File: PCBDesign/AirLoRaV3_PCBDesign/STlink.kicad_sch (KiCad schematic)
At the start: 1 part, among them J6 UART2

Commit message: Update circiut
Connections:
- net 3.3V renamed +3.3V
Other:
- moved on the sheet: J6
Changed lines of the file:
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@@
 	(generator_version "8.0")
 	(paper "A4")
-	(rectangle
-		(start 96.52 54.61)
-		(end 130.81 78.74)
+	(wire
+		(pts
+			(xy 142.24 100.33) (xy 157.48 100.33)
+		)
 		(stroke
 			(width 0)
 			(type default)
 		)
+	)
+	(rectangle
+		(start 129.54 83.82)
+		(end 163.83 107.95)
+		(stroke
+			(width 0)
+			(type default)
+		)
 		(fill
 			(type none)
@@
 	(text "STLink"
 		(exclude_from_sim no)
-		(at 113.538 56.642 0)
+		(at 146.558 85.852 0)
 		(effects
 			(font
@@
 	(hierarchical_label "T_SWCLK"
 		(shape input)
-		(at 115.57 69.85 0)
+		(at 142.24 97.79 0)
 		(fields_autoplaced yes)
 		(effects
@@
 	(hierarchical_label "T_SWDIO"
 		(shape input)
-		(at 115.57 67.31 0)
+		(at 142.24 95.25 0)
 		(fields_autoplaced yes)
 		(effects
@@
 		)
 	)
-	(hierarchical_label "3.3V"
-		(shape input)
-		(at 115.57 72.39 0)
-		(fields_autoplaced yes)
-		(effects
-			(font
-				(size 1.27 1.27)
-			)
-			(justify left)
-		)
-	)
 	(symbol
 		(lib_id "Connector:Screw_Terminal_01x04")
-		(at 110.49 72.39 180)
+		(at 137.16 100.33 180)
 		(unit 1)
 		(exclude_from_sim no)
@@
 		(fields_autoplaced yes)
 		(property "Reference" "J6"
-			(at 110.49 60.96 0)
+			(at 137.16 88.9 0)
 			(effects
 				(font
@@
 		)
 		(property "Value" "UART2"
-			(at 110.49 63.5 0)
+			(at 137.16 91.44 0)
 			(effects
 				(font
@@
 		)
 		(property "Footprint" "Connector_JST:JST_XH_B4B-XH-A_1x04_P2.50mm_Vertical"
-			(at 110.49 72.39 0)
+			(at 137.16 100.33 0)
 			(effects
 				(font
@@
 		)
 		(property "Datasheet" "~"
-			(at 110.49 72.39 0)
+			(at 137.16 100.33 0)
 			(effects
 				(font
@@
 		)
 		(property "Description" ""
-			(at 110.49 72.39 0)
+			(at 137.16 100.33 0)
 			(effects
 				(font
@@
 	(symbol
 		(lib_id "power:GND")
-		(at 115.57 74.93 90)
+		(at 142.24 102.87 90)
 		(unit 1)
 		(exclude_from_sim no)
@@
 		(fields_autoplaced yes)
 		(property "Reference" "#PWR043"
-			(at 121.92 74.93 0)
+			(at 148.59 102.87 0)
 			(effects
 				(font
@@
 		)
 		(property "Value" "GND"
-			(at 119.38 74.9299 90)
+			(at 146.05 102.8699 90)
 			(effects
 				(font
@@
 		)
 		(property "Footprint" ""
-			(at 115.57 74.93 0)
+			(at 142.24 102.87 0)
 			(effects
 				(font
@@
 		)
 		(property "Datasheet" ""
-			(at 115.57 74.93 0)
+			(at 142.24 102.87 0)
 			(effects
 				(font
@@
 		)
 		(property "Description" "Power symbol creates a global label with name \"GND\" , ground"
-			(at 115.57 74.93 0)
+			(at 142.24 102.87 0)
 			(effects
 				(font
@@
 					(unit 1)
 				)
+			)
+		)
+	)
+	(symbol
+		(lib_id "power:+3.3V")
+		(at 157.48 100.33 0)
+		(unit 1)
+		(exclude_from_sim no)
+		(in_bom yes)
+		(on_board yes)
+		(dnp no)
+		(fields_autoplaced yes)
+		(property "Reference" "#PWR044"
+			(at 157.48 104.14 0)
+			(effects
+				(font
+					(size 1.27 1.27)
+				)
+				(hide yes)
+			)
+		)
+		(property "Value" "+3.3V"
+			(at 157.48 95.25 0)
+			(effects
+				(font
+					(size 1.27 1.27)
+				)
+			)
+		)
+		(property "Footprint" ""
+			(at 157.48 100.33 0)
+			(effects
+				(font
+					(size 1.27 1.27)
+				)
+				(hide yes)
+			)
+		)
+		(property "Datasheet" ""
+			(at 157.48 100.33 0)
+			(effects
+				(font
+					(size 1.27 1.27)
+				)
+				(hide yes)
+			)
+		)
+		(property "Description" "Power symbol creates a global label with name \"+3.3V\""
+			(at 157.48 100.33 0)
+			(effects
+				(font
+					(size 1.27 1.27)
+				)
+				(hide yes)
+			)
+		)
+		(pin "1"
+		)
+		(instances
+			(project "airlora-kicad"
+				(path "/59d971df-d6c1-4ef7-a085-bf08b7b16047/be77b740-d58b-414b-97ce-61f1d1685314/0fe76900-3fef-41a8-aa6f-27268a6f6f64"
+					(reference "#PWR044")
+					(unit 1)
+				)

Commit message: Update PCB layout
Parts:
- renumbered J6 to J7
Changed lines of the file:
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@@
 		(dnp no)
 		(fields_autoplaced yes)
-		(property "Reference" "J6"
+		(property "Reference" "J7"
 			(at 137.16 88.9 0)
 			(effects
@@
 			(project "airlora-kicad"
 				(path "/59d971df-d6c1-4ef7-a085-bf08b7b16047/be77b740-d58b-414b-97ce-61f1d1685314/0fe76900-3fef-41a8-aa6f-27268a6f6f64"
-					(reference "J6")
+					(reference "J7")
 					(unit 1)
 				)

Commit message: Update schematic
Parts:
- added SW2: SW_Slide_DPDT, Button_Switch_THT:SW_E-Switch_EG1271_SPDT, symbol Switch:SW_Slide_DPDT
- renumbered J7 to J8
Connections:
- net T_SWCLK: now also SW2.6 (C); no longer J8.3 (Pin_3)
- net T_SWDIO: now also SW2.1 (A); no longer J8.4 (Pin_4)
- new net: J8.3 (Pin_3), SW2.2 (B)
- new net: J8.4 (Pin_4), SW2.5 (B)
- new net T_SWCLK1: SW2.4 (A)
- new net T_SWDIO1: SW2.3 (C)
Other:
- moved on the sheet: J8
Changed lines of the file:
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@@
 	(wire
 		(pts
-			(xy 142.24 100.33) (xy 157.48 100.33)
+			(xy 147.32 77.47) (xy 147.32 85.09)
+		)
+		(stroke
+			(width 0)
+			(type default)
+		)
+	)
+	(wire
+		(pts
+			(xy 147.32 85.09) (xy 139.7 85.09)
+		)
+		(stroke
+			(width 0)
+			(type default)
+		)
+	)
+	(wire
+		(pts
+			(xy 147.32 88.9) (xy 163.83 88.9)
+		)
+		(stroke
+			(width 0)
+			(type default)
+		)
+	)
+	(wire
+		(pts
+			(xy 147.32 87.63) (xy 139.7 87.63)
+		)
+		(stroke
+			(width 0)
+			(type default)
+		)
+	)
+	(wire
+		(pts
+			(xy 186.69 88.9) (xy 186.69 77.47)
+		)
+		(stroke
+			(width 0)
+			(type default)
+		)
+	)
+	(wire
+		(pts
+			(xy 186.69 77.47) (xy 147.32 77.47)
+		)
+		(stroke
+			(width 0)
+			(type default)
+		)
+	)
+	(wire
+		(pts
+			(xy 147.32 88.9) (xy 147.32 87.63)
+		)
+		(stroke
+			(width 0)
+			(type default)
+		)
+	)
+	(wire
+		(pts
+			(xy 173.99 88.9) (xy 186.69 88.9)
 		)
 		(stroke
@@
 	)
 	(rectangle
-		(start 129.54 83.82)
-		(end 163.83 107.95)
+		(start 126.365 66.04)
+		(end 191.135 100.33)
 		(stroke
 			(width 0)
@@
 	(text "STLink"
 		(exclude_from_sim no)
-		(at 146.558 85.852 0)
+		(at 159.766 72.644 0)
 		(effects
 			(font
@@
 		)
 	)
-	(hierarchical_label "T_SWCLK"
+	(hierarchical_label "T_SWCLK1"
 		(shape input)
-		(at 142.24 97.79 0)
+		(at 173.99 93.98 0)
 		(fields_autoplaced yes)
 		(effects
@@
 		)
 	)
-	(hierarchical_label "T_SWDIO"
+	(hierarchical_label "T_SWCLK"
 		(shape input)
-		(at 142.24 95.25 0)
+		(at 173.99 83.82 0)
 		(fields_autoplaced yes)
 		(effects
@@
 		)
 	)
+	(hierarchical_label "T_SWDIO"
+		(shape input)
+		(at 163.83 83.82 180)
+		(fields_autoplaced yes)
+		(effects
+			(font
+				(size 1.27 1.27)
+			)
+			(justify right)
+		)
+	)
+	(hierarchical_label "T_SWDIO1"
+		(shape input)
+		(at 163.83 93.98 180)
+		(fields_autoplaced yes)
+		(effects
+			(font
+				(size 1.27 1.27)
+			)
+			(justify right)
+		)
+	)
 	(symbol
 		(lib_id "Connector:Screw_Terminal_01x04")
-		(at 137.16 100.33 180)
+		(at 134.62 90.17 180)
 		(unit 1)
 		(exclude_from_sim no)
@@
 		(dnp no)
 		(fields_autoplaced yes)
-		(property "Reference" "J7"
-			(at 137.16 88.9 0)
+		(property "Reference" "J8"
+			(at 134.62 78.74 0)
 			(effects
 				(font
@@
 		)
 		(property "Value" "UART2"
-			(at 137.16 91.44 0)
+			(at 134.62 81.28 0)
 			(effects
 				(font
@@
 		)
 		(property "Footprint" "Connector_JST:JST_XH_B4B-XH-A_1x04_P2.50mm_Vertical"
-			(at 137.16 100.33 0)
+			(at 134.62 90.17 0)
 			(effects
 				(font
@@
 		)
 		(property "Datasheet" "~"
-			(at 137.16 100.33 0)
+			(at 134.62 90.17 0)
 			(effects
 				(font
@@
 		)
 		(property "Description" ""
-			(at 137.16 100.33 0)
+			(at 134.62 90.17 0)
 			(effects
 				(font
@@
 		)
 		(property "MANUFACTURER" ""
-			(at 137.16 100.33 0)
+			(at 134.62 90.17 0)
 			(effects
 				(font
@@
 		)
 		(property "MAXIMUM_PACKAGE_HEIGHT" ""
-			(at 137.16 100.33 0)
+			(at 134.62 90.17 0)
 			(effects
 				(font
@@
 		)
 		(property "PARTREV" ""
-			(at 137.16 100.33 0)
+			(at 134.62 90.17 0)
 			(effects
 				(font
@@
 		)
 		(property "STANDARD" ""
-			(at 137.16 100.33 0)
+			(at 134.62 90.17 0)
 			(effects
 				(font
@@
 			(project "airlora-kicad"
 				(path "/59d971df-d6c1-4ef7-a085-bf08b7b16047/be77b740-d58b-414b-97ce-61f1d1685314/0fe76900-3fef-41a8-aa6f-27268a6f6f64"
-					(reference "J7")
+					(reference "J8")
 					(unit 1)
 				)
@@
 	(symbol
 		(lib_id "power:GND")
-		(at 142.24 102.87 90)
+		(at 139.7 92.71 90)
 		(unit 1)
 		(exclude_from_sim no)
@@
 		(dnp no)
 		(fields_autoplaced yes)
-		(property "Reference" "#PWR043"
-			(at 148.59 102.87 0)
+		(property "Reference" "#PWR046"
+			(at 146.05 92.71 0)
 			(effects
 				(font
@@
 		)
 		(property "Value" "GND"
-			(at 146.05 102.8699 90)
+			(at 143.51 92.7099 90)
 			(effects
 				(font
@@
 		)
 		(property "Footprint" ""
-			(at 142.24 102.87 0)
+			(at 139.7 92.71 0)
 			(effects
 				(font
@@
 		)
 		(property "Datasheet" ""
-			(at 142.24 102.87 0)
+			(at 139.7 92.71 0)
 			(effects
 				(font
@@
 		)
 		(property "Description" "Power symbol creates a global label with name \"GND\" , ground"
-			(at 142.24 102.87 0)
+			(at 139.7 92.71 0)
 			(effects
 				(font
@@
 			(project "airlora-kicad"
 				(path "/59d971df-d6c1-4ef7-a085-bf08b7b16047/be77b740-d58b-414b-97ce-61f1d1685314/0fe76900-3fef-41a8-aa6f-27268a6f6f64"
-					(reference "#PWR043")
+					(reference "#PWR046")
 					(unit 1)
 				)
@@
 	(symbol
 		(lib_id "power:+3.3V")
-		(at 157.48 100.33 0)
+		(at 139.7 90.17 270)
 		(unit 1)
 		(exclude_from_sim no)
@@
 		(dnp no)
 		(fields_autoplaced yes)
-		(property "Reference" "#PWR044"
-			(at 157.48 104.14 0)
+		(property "Reference" "#PWR045"
+			(at 135.89 90.17 0)
 			(effects
 				(font
@@
 		)
 		(property "Value" "+3.3V"
-			(at 157.48 95.25 0)
-			(effects
-				(font
-					(size 1.27 1.27)
-				)
+			(at 143.51 90.1699 90)
+			(effects
+				(font
+					(size 1.27 1.27)
+				)
+				(justify left)
 			)
 		)
 		(property "Footprint" ""
-			(at 157.48 100.33 0)
+			(at 139.7 90.17 0)
 			(effects
 				(font
@@
 		)
 		(property "Datasheet" ""
-			(at 157.48 100.33 0)
+			(at 139.7 90.17 0)
 			(effects
 				(font
@@
 		)
 		(property "Description" "Power symbol creates a global label with name \"+3.3V\""
-			(at 157.48 100.33 0)
+			(at 139.7 90.17 0)
 			(effects
 				(font
@@
 			(project "airlora-kicad"
 				(path "/59d971df-d6c1-4ef7-a085-bf08b7b16047/be77b740-d58b-414b-97ce-61f1d1685314/0fe76900-3fef-41a8-aa6f-27268a6f6f64"
-					(reference "#PWR044")
+					(reference "#PWR045")
 					(unit 1)
 				)
+			)
+		)
+	)
+	(symbol
+		(lib_id "Switch:SW_Slide_DPDT")
+		(at 168.91 88.9 0)
+		(unit 1)
+		(exclude_from_sim no)
+		(in_bom yes)
+		(on_board yes)
+		(dnp no)
+		(fields_autoplaced yes)
+		(property "Reference" "SW2"
+			(at 168.91 78.74 0)
+			(effects
+				(font
+					(size 1.27 1.27)
+				)
+			)
+		)
+		(property "Value" "SW_Slide_DPDT"
+			(at 168.91 81.28 0)
+			(effects
+				(font
+					(size 1.27 1.27)
+				)
+			)
+		)
+		(property "Footprint" "Button_Switch_THT:SW_E-Switch_EG1271_SPDT"
+			(at 182.88 83.82 0)
+			(effects
+				(font
+					(size 1.27 1.27)
+				)
+				(hide yes)
+			)
+		)
+		(property "Datasheet" "~"
+			(at 168.91 88.9 0)
+			(effects
+				(font
+					(size 1.27 1.27)
+				)
+				(hide yes)
+			)
+		)
+		(property "Description" "Slide Switch, dual pole double throw"
+			(at 168.91 88.9 0)
+			(effects
+				(font
+					(size 1.27 1.27)
+				)
+				(hide yes)
+			)
+		)
+		(pin "6"
+		)
+		(pin "4"
+		)
+		(pin "1"
+		)
+		(pin "3"
+		)
+		(pin "5"
+		)
+		(pin "2"
+		)
+		(instances
+			(project "airlora-kicad"
+				(path "/59d971df-d6c1-4ef7-a085-bf08b7b16047/be77b740-d58b-414b-97ce-61f1d1685314/0fe76900-3fef-41a8-aa6f-27268a6f6f64"
+					(reference "SW2")
+					(unit 1)
+				)

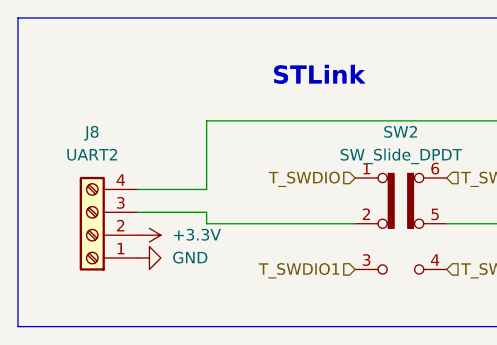
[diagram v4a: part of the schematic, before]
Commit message: Update circuit buck converter and sensor
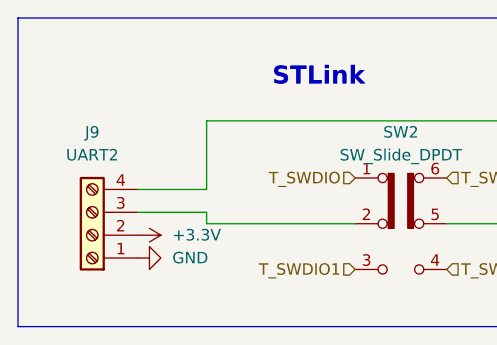
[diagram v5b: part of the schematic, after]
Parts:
- J9: renamed from J8; footprint Connector_JST:JST_XH_B4B-XH-A_1x04_P2.50mm_Vertical -> Connector_Molex:Molex_CLIK-Mate_502585-0470_1x04-1MP_P1.50mm_Horizontal
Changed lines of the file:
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@@
 		(dnp no)
 		(fields_autoplaced yes)
-		(property "Reference" "J8"
+		(property "Reference" "J9"
 			(at 134.62 78.74 0)
 			(effects
@@
 			)
 		)
-		(property "Footprint" "Connector_JST:JST_XH_B4B-XH-A_1x04_P2.50mm_Vertical"
+		(property "Footprint" "Connector_Molex:Molex_CLIK-Mate_502585-0470_1x04-1MP_P1.50mm_Horizontal"
 			(at 134.62 90.17 0)
 			(effects
@@
 			(project "airlora-kicad"
 				(path "/59d971df-d6c1-4ef7-a085-bf08b7b16047/be77b740-d58b-414b-97ce-61f1d1685314/0fe76900-3fef-41a8-aa6f-27268a6f6f64"
-					(reference "J8")
+					(reference "J9")
 					(unit 1)
 				)
@@
 		(dnp no)
 		(fields_autoplaced yes)
-		(property "Reference" "#PWR046"
+		(property "Reference" "#PWR051"
 			(at 146.05 92.71 0)
 			(effects
@@
 			(project "airlora-kicad"
 				(path "/59d971df-d6c1-4ef7-a085-bf08b7b16047/be77b740-d58b-414b-97ce-61f1d1685314/0fe76900-3fef-41a8-aa6f-27268a6f6f64"
-					(reference "#PWR046")
+					(reference "#PWR051")
 					(unit 1)
 				)
@@
 		(dnp no)
 		(fields_autoplaced yes)
-		(property "Reference" "#PWR045"
+		(property "Reference" "#PWR050"
 			(at 135.89 90.17 0)
 			(effects
@@
 			(project "airlora-kicad"
 				(path "/59d971df-d6c1-4ef7-a085-bf08b7b16047/be77b740-d58b-414b-97ce-61f1d1685314/0fe76900-3fef-41a8-aa6f-27268a6f6f64"
-					(reference "#PWR045")
+					(reference "#PWR050")
 					(unit 1)
 				)

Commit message: Update schematic
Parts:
- J9: footprint Connector_Molex:Molex_CLIK-Mate_502585-0470_1x04-1MP_P1.50mm_Horizontal -> Connector_JST:JST_XH_B4B-XH-A_1x04_P2.50mm_Vertical
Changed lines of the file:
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@@
 			)
 		)
-		(property "Footprint" "Connector_Molex:Molex_CLIK-Mate_502585-0470_1x04-1MP_P1.50mm_Horizontal"
+		(property "Footprint" "Connector_JST:JST_XH_B4B-XH-A_1x04_P2.50mm_Vertical"
 			(at 134.62 90.17 0)
 			(effects

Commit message: Update PCB
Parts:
- renumbered J9 to J11
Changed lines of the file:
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@@
 		(dnp no)
 		(fields_autoplaced yes)
-		(property "Reference" "J9"
+		(property "Reference" "J11"
 			(at 134.62 78.74 0)
 			(effects
@@
 			(project "airlora-kicad"
 				(path "/59d971df-d6c1-4ef7-a085-bf08b7b16047/be77b740-d58b-414b-97ce-61f1d1685314/0fe76900-3fef-41a8-aa6f-27268a6f6f64"
-					(reference "J9")
+					(reference "J11")
 					(unit 1)
 				)
@@
 		(dnp no)
 		(fields_autoplaced yes)
-		(property "Reference" "#PWR051"
+		(property "Reference" "#PWR058"
 			(at 146.05 92.71 0)
 			(effects
@@
 			(project "airlora-kicad"
 				(path "/59d971df-d6c1-4ef7-a085-bf08b7b16047/be77b740-d58b-414b-97ce-61f1d1685314/0fe76900-3fef-41a8-aa6f-27268a6f6f64"
-					(reference "#PWR051")
+					(reference "#PWR058")
 					(unit 1)
 				)
@@
 		(dnp no)
 		(fields_autoplaced yes)
-		(property "Reference" "#PWR050"
+		(property "Reference" "#PWR057"
 			(at 135.89 90.17 0)
 			(effects
@@
 			(project "airlora-kicad"
 				(path "/59d971df-d6c1-4ef7-a085-bf08b7b16047/be77b740-d58b-414b-97ce-61f1d1685314/0fe76900-3fef-41a8-aa6f-27268a6f6f64"
-					(reference "#PWR050")
+					(reference "#PWR057")
 					(unit 1)
 				)
